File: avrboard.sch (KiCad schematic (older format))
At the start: 20 parts, among them IC1 ATMEGA328P-P, P1 FTDI, P2 ICSP, SW1 RESET, U1 7805, X1 16MHz

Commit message: Connect AREF to +5V.
No sensible way to route AREF, so for now the compromise is to just route
it to +5V so the ADC can be *usable* when configured to use an external
voltage source (e.g. for testing after programming) while not being
particularly accurate (since this is going to be noisy.)

Given that the primary purpose of this board is programming and then
post-programming brief testing, with the chip ultimately ending up in
a dedicated PCB design, this seems like a reasonable compromise.
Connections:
- net AREF is gone; now on net +5V: PP1.1
- net +5V: now also IC1.21 (AREF)

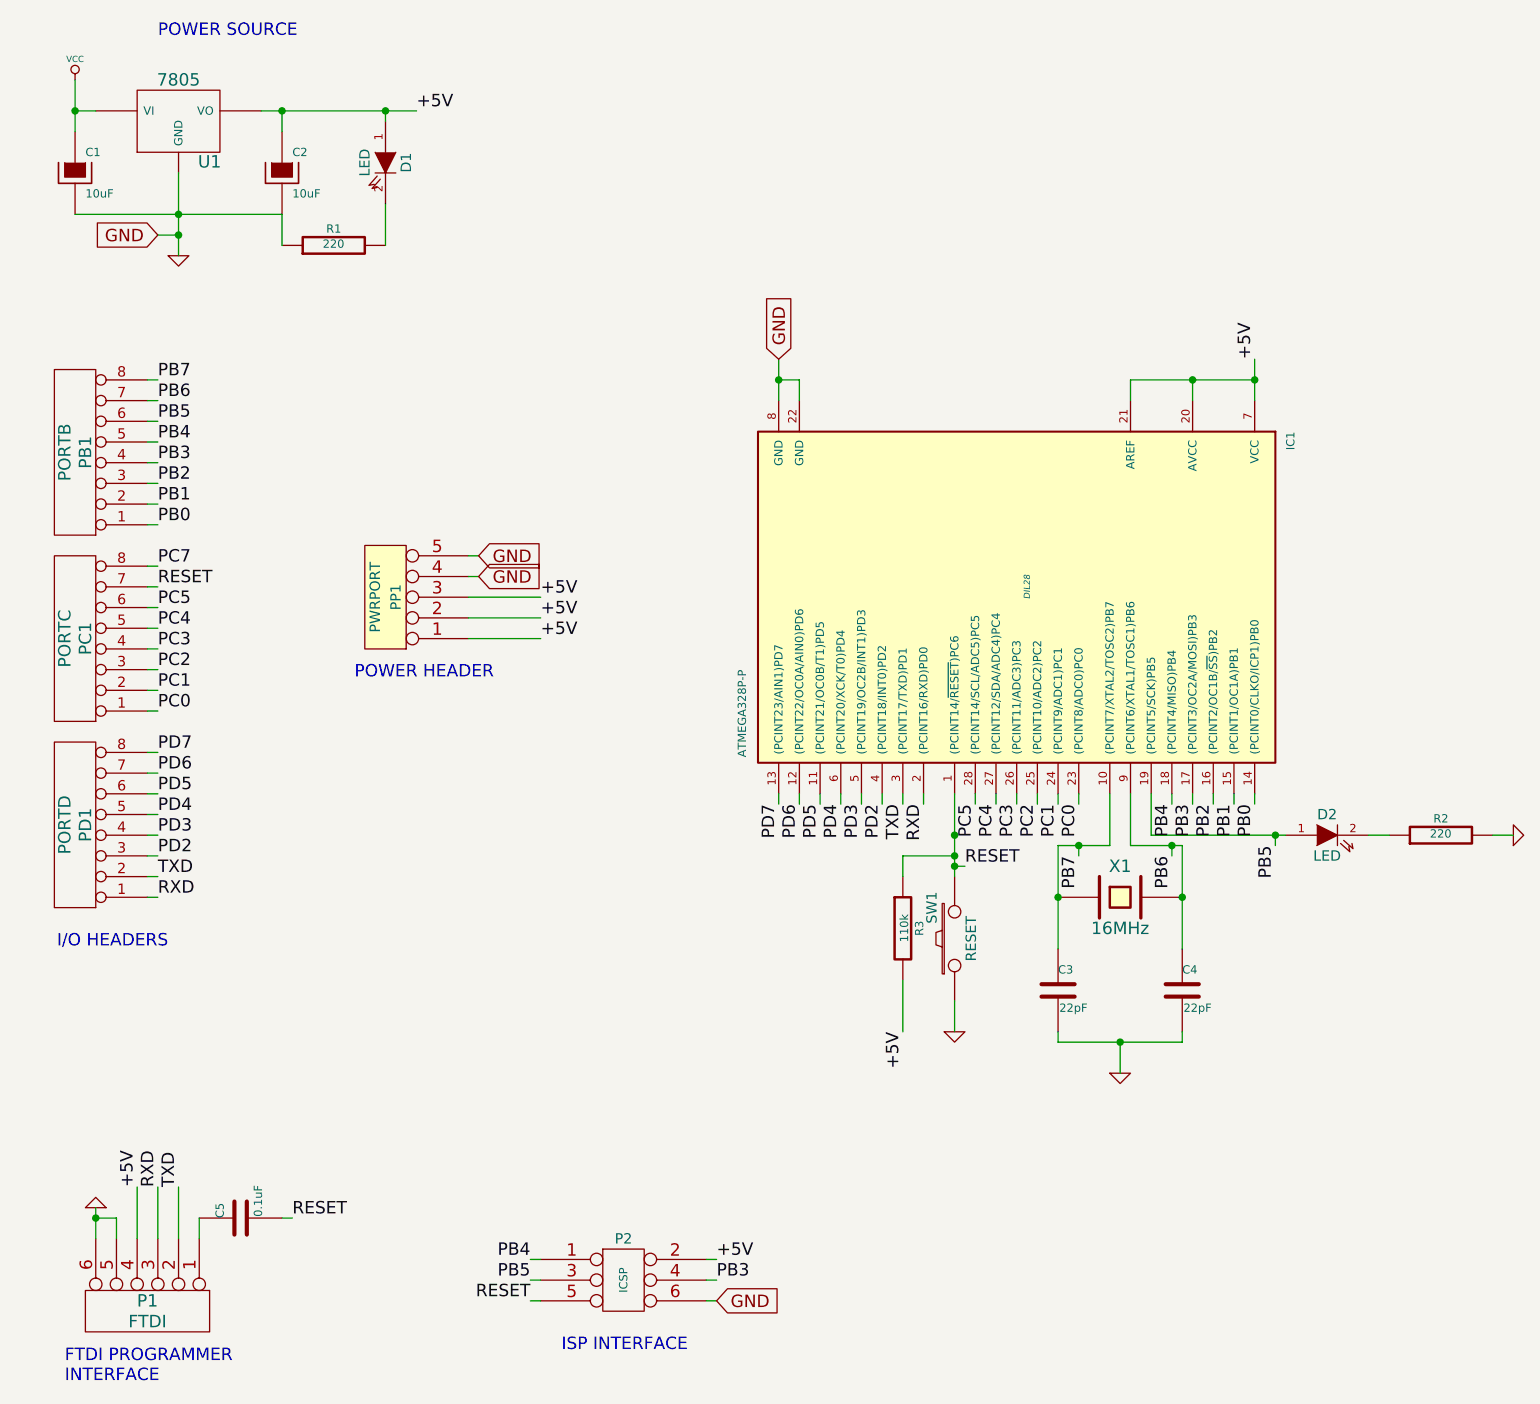
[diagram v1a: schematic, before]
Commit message: Remove the power regulator from the design.
Since this board is primarily for programming, it's fine to just get
power from the ICSP or FTDI headers in most cases, which should already
be regulated to 5V.

There was nowhere in the design for the power barrel jack to go anyway,
so this saves a little more space and also allows the ICSP header to move
closer to the SPI pins and thus fix some of the more awkward routes
from the previous iteration.
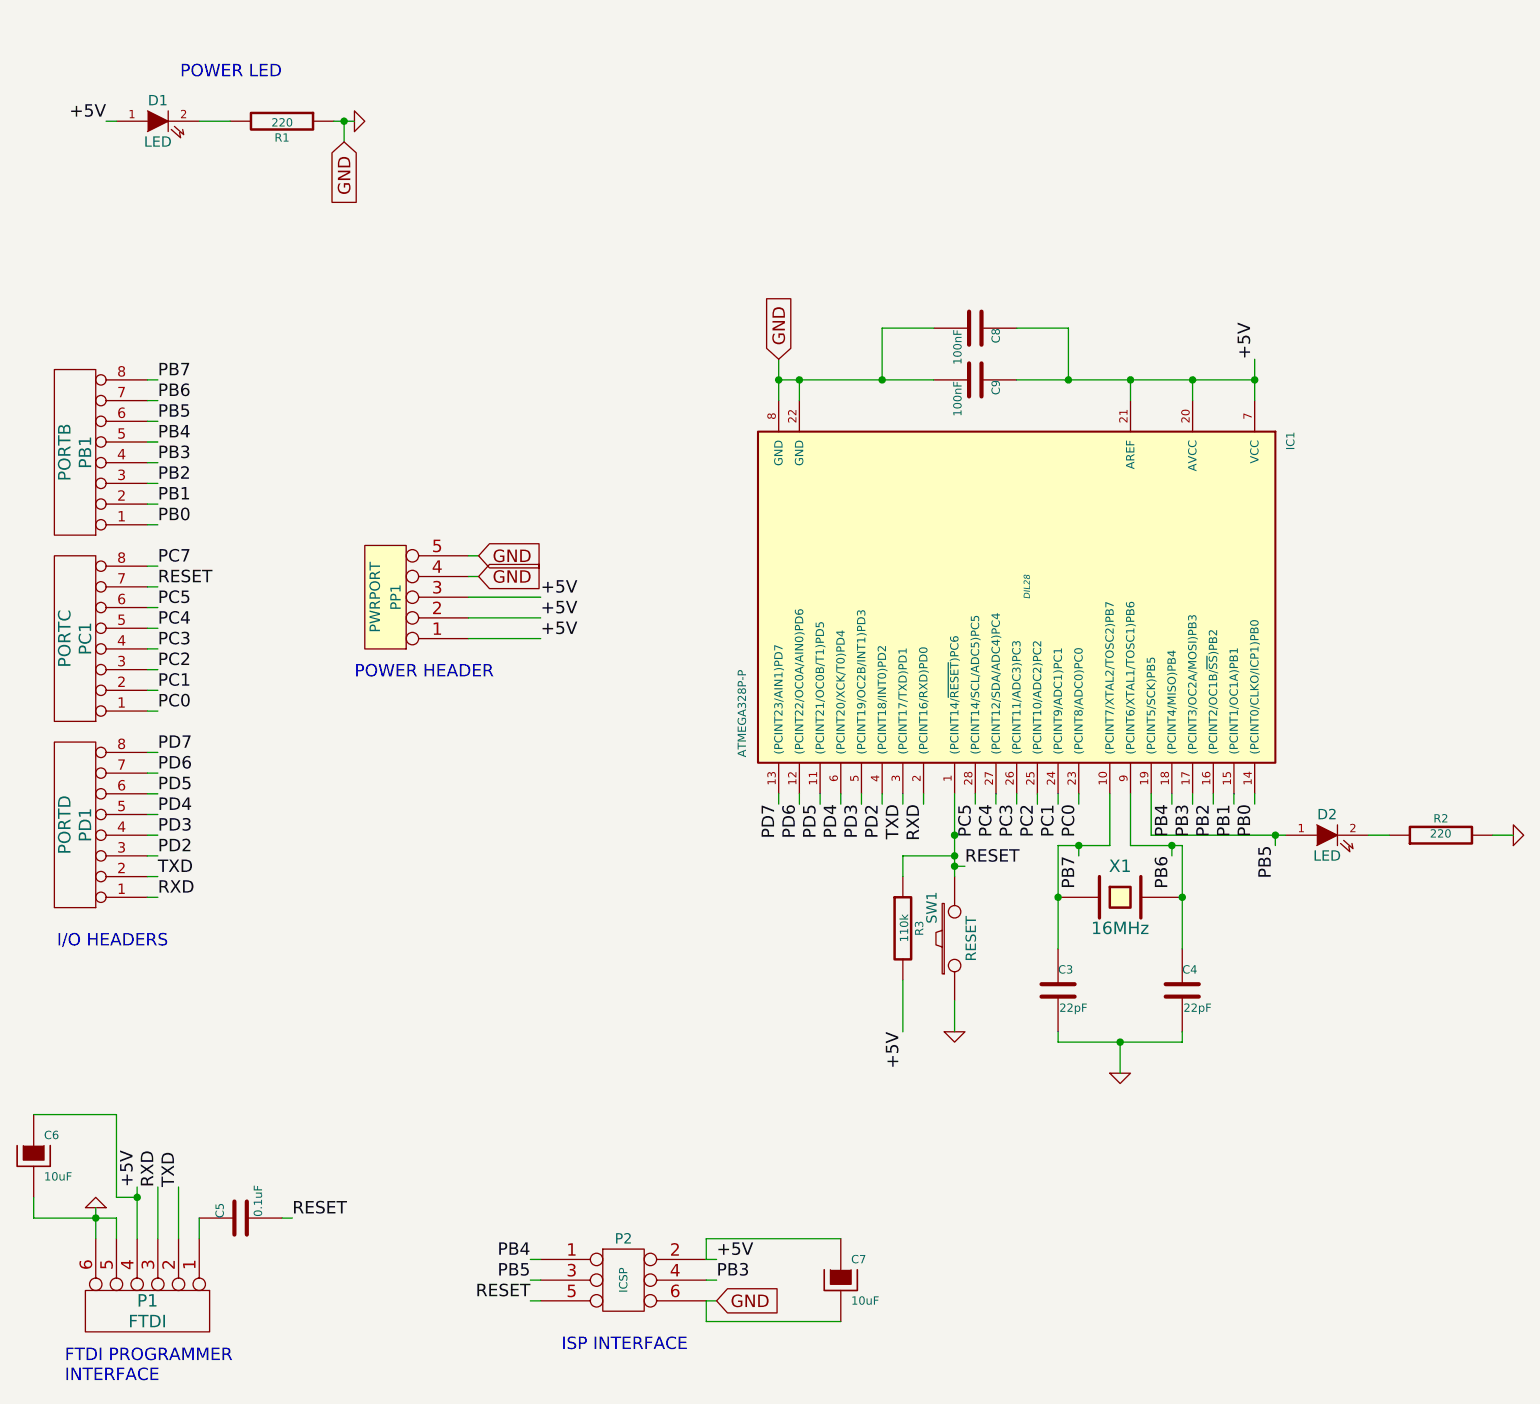
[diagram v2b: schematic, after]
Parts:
- removed C1, C2: 10uF, symbol CP
- removed U1: 7805, symbol 7805
- added C6, C7: 10uF, symbol CP
- added C8, C9: 100nF, symbol C
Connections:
- net +5V: now also C6.1, C7.1, C8.1, C9.1
- net GND: now also C6.2, C7.2, C8.2, C9.2
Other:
- note added: "POWER LED"
- note removed: "POWER SOURCE"
- moved on the sheet: D1, R1
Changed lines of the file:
@@
 $EndDescr
-$Comp
-L 7805 U1
-U 1 1 534CB6E6
-P 1650 1250
-F 0 "U1" H 1800 1054 60  0000 C CNN
-F 1 "7805" H 1650 1450 60  0000 C CNN
-F 2 "" H 1650 1250 60  0000 C CNN
-F 3 "" H 1650 1250 60  0000 C CNN
-	1    1650 1250
-	1    0    0    -1
-$EndComp
 $Comp
 L R R1
 U 1 1 534CB713
-P 2400 1850
-F 0 "R1" V 2480 1850 40  0000 C CNN
-F 1 "220" V 2407 1851 40  0000 C CNN
-F 2 "" V 2330 1850 30  0000 C CNN
-F 3 "" H 2400 1850 30  0000 C CNN
-	1    2400 1850
-	0    -1   -1   0
+P 2150 1250
+F 0 "R1" V 2230 1250 40  0000 C CNN
+F 1 "220" V 2157 1251 40  0000 C CNN
+F 2 "" V 2080 1250 30  0000 C CNN
+F 3 "" H 2150 1250 30  0000 C CNN
+	1    2150 1250
+	0    1    1    0
 $EndComp
 $Comp
@@
 $EndComp
 $Comp
-L CP C1
-U 1 1 534CB7BE
-P 1150 1500
-F 0 "C1" H 1200 1600 40  0000 L CNN
-F 1 "10uF" H 1200 1400 40  0000 L CNN
-F 2 "" H 1250 1350 30  0000 C CNN
-F 3 "" H 1150 1500 300 0000 C CNN
-	1    1150 1500
-	1    0    0    -1
-$EndComp
-$Comp
-L CP C2
-U 1 1 534CB7E4
-P 2150 1500
-F 0 "C2" H 2200 1600 40  0000 L CNN
-F 1 "10uF" H 2200 1400 40  0000 L CNN
-F 2 "" H 2250 1350 30  0000 C CNN
-F 3 "" H 2150 1500 300 0000 C CNN
-	1    2150 1500
-	1    0    0    -1
-$EndComp
-$Comp
 L CRYSTAL X1
 U 1 1 534CB845
@@
 L LED D1
 U 1 1 534CB9E9
-P 2650 1450
-F 0 "D1" H 2650 1550 50  0000 C CNN
-F 1 "LED" H 2650 1350 50  0000 C CNN
-F 2 "" H 2650 1450 60  0000 C CNN
-F 3 "" H 2650 1450 60  0000 C CNN
-	1    2650 1450
-	0    1    1    0
+P 1550 1250
+F 0 "D1" H 1550 1350 50  0000 C CNN
+F 1 "LED" H 1550 1150 50  0000 C CNN
+F 2 "" H 1550 1250 60  0000 C CNN
+F 3 "" H 1550 1250 60  0000 C CNN
+	1    1550 1250
+	1    0    0    -1
 $EndComp
 $Comp
@@
 $EndComp
 $Comp
-L VCC #PWR01
-U 1 1 534CBAF9
-P 1150 1050
-F 0 "#PWR01" H 1150 1150 30  0001 C CNN
-F 1 "VCC" H 1150 1150 30  0000 C CNN
-F 2 "" H 1150 1050 60  0000 C CNN
-F 3 "" H 1150 1050 60  0000 C CNN
-	1    1150 1050
-	1    0    0    -1
-$EndComp
-$Comp
-L GND #PWR02
+L GND #PWR3
 U 1 1 534CBB1B
-P 1650 1900
-F 0 "#PWR02" H 1650 1900 30  0001 C CNN
-F 1 "GND" H 1650 1830 30  0001 C CNN
-F 2 "" H 1650 1900 60  0000 C CNN
-F 3 "" H 1650 1900 60  0000 C CNN
-	1    1650 1900
-	1    0    0    -1
-$EndComp
-Text Label 2800 1200 0    60   ~ 0
-+5V
-Text GLabel 1550 1800 0    60   Input ~ 0
+P 2500 1250
+F 0 "#PWR3" H 2500 1250 30  0001 C CNN
+F 1 "GND" H 2500 1180 30  0001 C CNN
+F 2 "" H 2500 1250 60  0000 C CNN
+F 3 "" H 2500 1250 60  0000 C CNN
+	1    2500 1250
+	0    -1   -1   0
+$EndComp
+Text GLabel 2450 1350 3    60   Input ~ 0
 GND
 Text GLabel 4550 2400 1    60   Input ~ 0
@@
 $EndComp
 $Comp
-L GND #PWR03
+L GND #PWR5
 U 1 1 534CBD9C
 P 6200 5850
-F 0 "#PWR03" H 6200 5850 30  0001 C CNN
+F 0 "#PWR5" H 6200 5850 30  0001 C CNN
 F 1 "GND" H 6200 5780 30  0001 C CNN
 F 2 "" H 6200 5850 60  0000 C CNN
@@
 $EndComp
 $Comp
-L GND #PWR04
+L GND #PWR4
 U 1 1 534CC010
 P 5400 5650
-F 0 "#PWR04" H 5400 5650 30  0001 C CNN
+F 0 "#PWR4" H 5400 5650 30  0001 C CNN
 F 1 "GND" H 5400 5580 30  0001 C CNN
 F 2 "" H 5400 5650 60  0000 C CNN
@@
 +5V
 $Comp
-L GND #PWR05
+L GND #PWR6
 U 1 1 534CC16B
 P 8100 4700
-F 0 "#PWR05" H 8100 4700 30  0001 C CNN
+F 0 "#PWR6" H 8100 4700 30  0001 C CNN
 F 1 "GND" H 8100 4630 30  0001 C CNN
 F 2 "" H 8100 4700 60  0000 C CNN
@@
 $EndComp
 $Comp
-L GND #PWR06
+L GND #PWR1
 U 1 1 534D4B29
 P 1250 6500
-F 0 "#PWR06" H 1250 6500 30  0001 C CNN
+F 0 "#PWR1" H 1250 6500 30  0001 C CNN
 F 1 "GND" H 1250 6430 30  0001 C CNN
 F 2 "" H 1250 6500 60  0000 C CNN
@@
 Text Label 5450 4850 0    60   ~ 0
 RESET
-Text Notes 1550 850  0    60   ~ 0
-POWER SOURCE
+Text Notes 2150 1050 2    60   ~ 0
+POWER LED
 Text Notes 1100 7350 0    60   ~ 0
 FTDI PROGRAMMER\nINTERFACE
@@
 ISP INTERFACE
 Wire Wire Line
-	1650 1500 1650 1900
-Wire Wire Line
-	1150 1700 2150 1700
-Connection ~ 1650 1700
-Wire Wire Line
-	2150 1200 2150 1300
-Wire Wire Line
-	1250 1200 1150 1200
-Wire Wire Line
-	1150 1050 1150 1300
-Connection ~ 2150 1200
-Wire Wire Line
-	2650 1200 2650 1250
-Wire Wire Line
-	2650 1650 2650 1850
-Wire Wire Line
-	2150 1700 2150 1850
-Connection ~ 1150 1200
-Connection ~ 2650 1200
-Wire Wire Line
-	2050 1200 2800 1200
-Wire Wire Line
-	1550 1800 1650 1800
-Connection ~ 1650 1800
-Wire Wire Line
 	4550 2400 4550 2600
 Wire Wire Line
-	4550 2500 4650 2500
+	4550 2500 5300 2500
 Wire Wire Line
 	4650 2500 4650 2600
@@
 	6850 2400 6850 2600
 Wire Wire Line
-	6250 2500 6850 2500
+	5700 2500 6850 2500
 Wire Wire Line
 	6550 2500 6550 2600
 Connection ~ 6850 2500
 Wire Wire Line
-	6150 4500 6150 4750
-Wire Wire Line
-	6150 4750 5900 4750
+	6150 4750 6150 4500
+Wire Wire Line
+	5900 4750 6150 4750
 Wire Wire Line
 	5900 4750 5900 5250
@@
 	8000 4700 8100 4700
 Wire Wire Line
-	1250 6650 1250 6500
-Wire Wire Line
-	1450 6650 1450 6400
+	1250 6500 1250 6650
+Wire Wire Line
+	1450 6400 1450 6650
 Wire Wire Line
 	1550 6650 1550 6400
@@
 Connection ~ 5400 4700
 Wire Wire Line
-	1350 6650 1350 6550
-Wire Wire Line
-	1350 6550 1250 6550
+	1350 6550 1350 6650
+Wire Wire Line
+	950  6550 1350 6550
 Connection ~ 1250 6550
 Wire Wire Line
@@
 	6250 2500 6250 2600
 Connection ~ 6550 2500
+$Comp
+L CP C6
+U 1 1 5353F975
+P 950 6250
+F 0 "C6" H 1000 6350 40  0000 L CNN
+F 1 "10uF" H 1000 6150 40  0000 L CNN
+F 2 "" H 1050 6100 30  0000 C CNN
+F 3 "" H 950 6250 300 0000 C CNN
+	1    950  6250
+	1    0    0    -1
+$EndComp
+Wire Wire Line
+	1450 6450 1350 6450
+Wire Wire Line
+	1350 6450 1350 6050
+Wire Wire Line
+	1350 6050 950  6050
+Connection ~ 1450 6450
+Wire Wire Line
+	950  6550 950  6450
+$Comp
+L CP C7
+U 1 1 5353FA96
+P 4850 6850
+F 0 "C7" H 4900 6950 40  0000 L CNN
+F 1 "10uF" H 4900 6750 40  0000 L CNN
+F 2 "" H 4950 6700 30  0000 C CNN
+F 3 "" H 4850 6850 300 0000 C CNN
+	1    4850 6850
+	1    0    0    -1
+$EndComp
+Wire Wire Line
+	4200 6750 4200 6650
+Wire Wire Line
+	4200 6650 4850 6650
+Wire Wire Line
+	4850 7050 4200 7050
+Wire Wire Line
+	4200 7050 4200 6950
+$Comp
+L C C9
+U 1 1 5353FBAB
+P 5500 2500
+F 0 "C9" H 5500 2600 40  0000 L CNN
+F 1 "100nF" H 5506 2415 40  0000 L CNN
+F 2 "" H 5538 2350 30  0000 C CNN
+F 3 "" H 5500 2500 60  0000 C CNN
+	1    5500 2500
+	0    1    1    0
+$EndComp
+$Comp
+L C C8
+U 1 1 5353FBB6
+P 5500 2250
+F 0 "C8" H 5500 2350 40  0000 L CNN
+F 1 "100nF" H 5506 2165 40  0000 L CNN
+F 2 "" H 5538 2100 30  0000 C CNN
+F 3 "" H 5500 2250 60  0000 C CNN
+	1    5500 2250
+	0    1    1    0
+$EndComp
+Connection ~ 6250 2500
+Connection ~ 4650 2500
+Wire Wire Line
+	5300 2250 5050 2250
+Wire Wire Line
+	5050 2250 5050 2500
+Connection ~ 5050 2500
+Wire Wire Line
+	5700 2250 5950 2250
+Wire Wire Line
+	5950 2250 5950 2500
+Connection ~ 5950 2500
+Wire Wire Line
+	1750 1250 1900 1250
+Wire Wire Line
+	2400 1250 2500 1250
+Wire Wire Line
+	2450 1350 2450 1250
+Connection ~ 2450 1250
+Text Label 1300 1250 2    60   ~ 0
++5V
+Wire Wire Line
+	1300 1250 1350 1250
 $EndSCHEMATC
